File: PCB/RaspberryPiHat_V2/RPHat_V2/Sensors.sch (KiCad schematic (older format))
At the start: 19 parts, among them IC1 TXB0108YZPR2, J2 Hall effect connector Right, J3 Halleffect Connector Left, U1 BME680, U2 INA219AxD, U3 ICM-20948, U4 GY-NEO6MV2

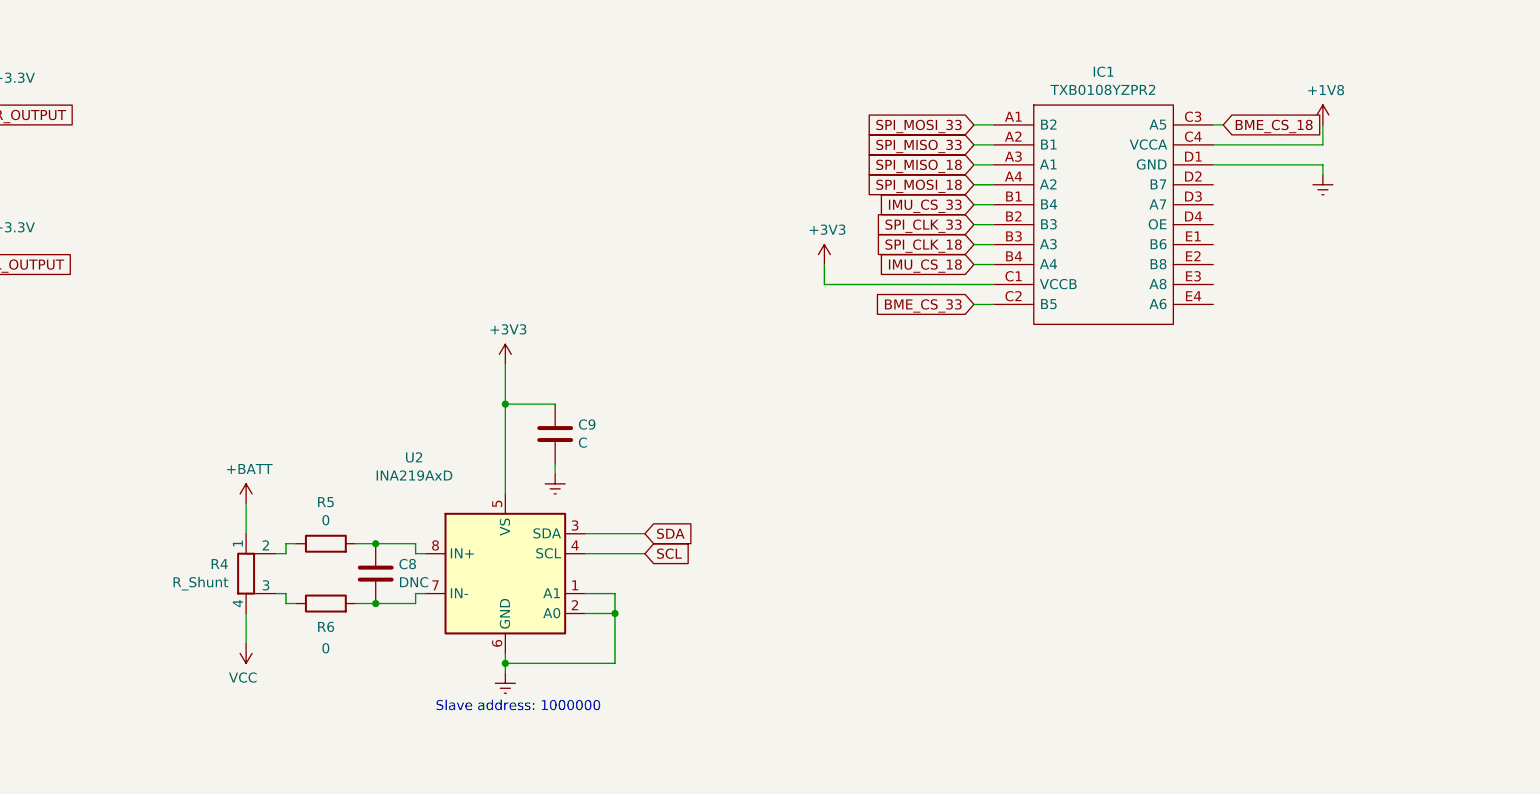
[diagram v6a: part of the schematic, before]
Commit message: Added footprints to all componetns
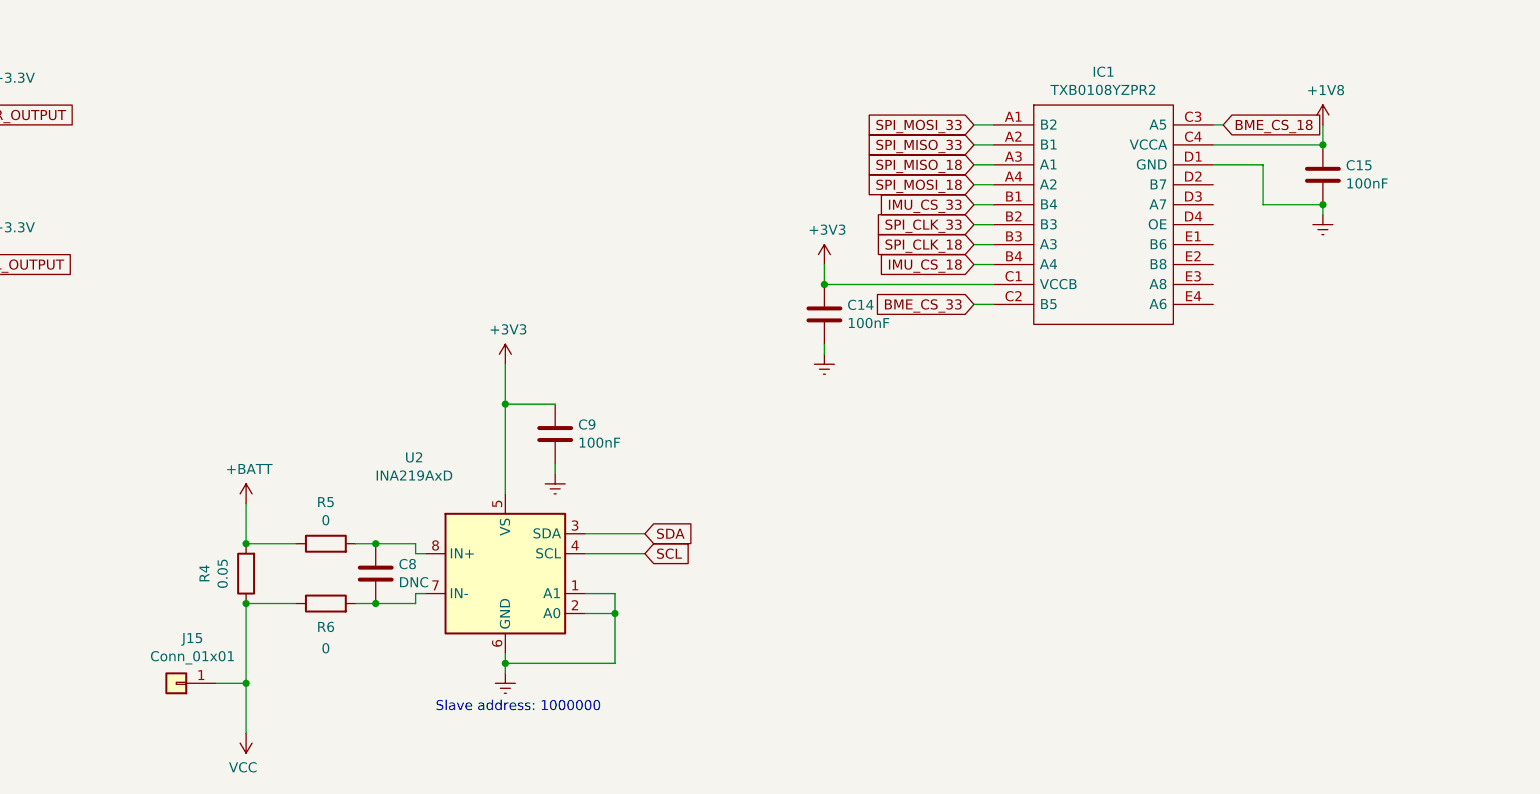
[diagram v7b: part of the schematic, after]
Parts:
- removed R4: R_Shunt, symbol Device:R_Shunt
- added C14, C15: 100nF, Capacitor_SMD:C_0603_1608Metric_Pad1.08x0.95mm_HandSolder, symbol Device:C
- added J15: Conn_01x01, Connector_Pin:Pin_D1.3mm_L11.0mm, symbol Connector_Generic:Conn_01x01
- added R4: 0.05, User:CSS2H-3920, symbol Device:R
- C10, C11, C12, C6, C7: footprint Capacitor_SMD:C_0805_2012Metric_Pad1.18x1.45mm_HandSolder -> Capacitor_SMD:C_0603_1608Metric_Pad1.08x0.95mm_HandSolder
- C8: footprint (none) -> Capacitor_SMD:C_0603_1608Metric_Pad1.08x0.95mm_HandSolder
- C9: value C -> 100nF; footprint (none) -> Capacitor_SMD:C_0603_1608Metric_Pad1.08x0.95mm_HandSolder
- IC1: footprint BGA20C50P4X5_189X239X50 -> TXB0108YZPR2:BGA20C50P4X5_189X239X50
- R5, R6: footprint (none) -> Resistor_SMD:R_0603_1608Metric_Pad0.98x0.95mm_HandSolder
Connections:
- net +1V8: now also C15.1
- net +3V3: now also C14.1
- net +BATT: now also R5.1, R4.2
- net GNDREF: now also C14.2, C15.2
- net VCC: now also R6.1, J15.1 (Pin_1), R4.1
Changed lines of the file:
@@
 F 0 "C7" H 1615 1496 50  0000 L CNN
 F 1 "100nF" H 1615 1405 50  0000 L CNN
-F 2 "Capacitor_SMD:C_0805_2012Metric_Pad1.18x1.45mm_HandSolder" H 1538 1300 50  0001 C CNN
+F 2 "Capacitor_SMD:C_0603_1608Metric_Pad1.08x0.95mm_HandSolder" H 1538 1300 50  0001 C CNN
 F 3 "~" H 1500 1450 50  0001 C CNN
 	1    1500 1450
@@
 F 0 "C6" H 1165 1496 50  0000 L CNN
 F 1 "100nF" H 1165 1405 50  0000 L CNN
-F 2 "Capacitor_SMD:C_0805_2012Metric_Pad1.18x1.45mm_HandSolder" H 1088 1300 50  0001 C CNN
+F 2 "Capacitor_SMD:C_0603_1608Metric_Pad1.08x0.95mm_HandSolder" H 1088 1300 50  0001 C CNN
 F 3 "~" H 1050 1450 50  0001 C CNN
 	1    1050 1450
@@
 F 0 "C11" H 7815 2246 50  0000 L CNN
 F 1 "100nF" H 7815 2155 50  0000 L CNN
-F 2 "Capacitor_SMD:C_0805_2012Metric_Pad1.18x1.45mm_HandSolder" H 7738 2050 50  0001 C CNN
+F 2 "Capacitor_SMD:C_0603_1608Metric_Pad1.08x0.95mm_HandSolder" H 7738 2050 50  0001 C CNN
 F 3 "~" H 7700 2200 50  0001 C CNN
 	1    7700 2200
@@
 F 0 "C10" H 7765 1446 50  0000 L CNN
 F 1 "100nF" H 7765 1355 50  0000 L CNN
-F 2 "Capacitor_SMD:C_0805_2012Metric_Pad1.18x1.45mm_HandSolder" H 7688 1250 50  0001 C CNN
+F 2 "Capacitor_SMD:C_0603_1608Metric_Pad1.08x0.95mm_HandSolder" H 7688 1250 50  0001 C CNN
 F 3 "~" H 7650 1400 50  0001 C CNN
 	1    7650 1400
@@
 F 0 "C12" H 8215 1446 50  0000 L CNN
 F 1 "100nF" H 8215 1355 50  0000 L CNN
-F 2 "Capacitor_SMD:C_0805_2012Metric_Pad1.18x1.45mm_HandSolder" H 8138 1250 50  0001 C CNN
+F 2 "Capacitor_SMD:C_0603_1608Metric_Pad1.08x0.95mm_HandSolder" H 8138 1250 50  0001 C CNN
 F 3 "~" H 8100 1400 50  0001 C CNN
 	1    8100 1400
@@
 F 0 "IC1" H 7000 4065 50  0000 C CNN
 F 1 "TXB0108YZPR2" H 7000 3974 50  0000 C CNN
-F 2 "BGA20C50P4X5_189X239X50" H 7400 3900 50  0001 L CNN
+F 2 "TXB0108YZPR2:BGA20C50P4X5_189X239X50" H 7400 3900 50  0001 L CNN
 F 3 "http://www.ti.com/lit/gpn/TXB0108" H 7400 3800 50  0001 L CNN
 F 4 "8-Bit Bidirectional Voltage-Level Shifter with Auto Direction Sensing and +/-15-kV ESD Protect" H 7400 3700 50  0001 L CNN "Description"
@@
 Wire Wire Line
 	8100 3900 8100 3800
-$Comp
-L power:GNDREF #PWR0132
-U 1 1 609C7438
-P 8100 4050
-F 0 "#PWR0132" H 8100 3800 50  0001 C CNN
-F 1 "GNDREF" H 8105 3877 50  0001 C CNN
-F 2 "" H 8100 4050 50  0001 C CNN
-F 3 "" H 8100 4050 50  0001 C CNN
-	1    8100 4050
-	1    0    0    -1
-$EndComp
-Wire Wire Line
-	8100 4000 8100 4050
 Wire Wire Line
 	7550 3900 8100 3900
-Wire Wire Line
-	7550 4000 8100 4000
 Text GLabel 6350 4000 0    50   Input ~ 0
 SPI_MISO_18
@@
 P 4250 5350
 F 0 "C9" H 4365 5396 50  0000 L CNN
-F 1 "C" H 4365 5305 50  0000 L CNN
-F 2 "" H 4288 5200 50  0001 C CNN
+F 1 "100nF" H 4365 5305 50  0000 L CNN
+F 2 "Capacitor_SMD:C_0603_1608Metric_Pad1.08x0.95mm_HandSolder" H 4288 5200 50  0001 C CNN
 F 3 "~" H 4250 5350 50  0001 C CNN
 	1    4250 5350
@@
 	4250 5500 4250 5550
 $Comp
-L Device:R_Shunt R4
-U 1 1 60A2AE3C
-P 2700 6050
-F 0 "R4" H 2612 6096 50  0000 R CNN
-F 1 "R_Shunt" H 2612 6005 50  0000 R CNN
-F 2 "" V 2630 6050 50  0001 C CNN
-F 3 "~" H 2700 6050 50  0001 C CNN
-	1    2700 6050
-	1    0    0    -1
-$EndComp
-$Comp
 L Device:R R5
 U 1 1 60A32138
@@
 F 0 "R5" V 3307 5900 50  0000 C CNN
 F 1 "0" V 3216 5900 50  0000 C CNN
-F 2 "" V 3030 5900 50  0001 C CNN
+F 2 "Resistor_SMD:R_0603_1608Metric_Pad0.98x0.95mm_HandSolder" V 3030 5900 50  0001 C CNN
 F 3 "~" H 3100 5900 50  0001 C CNN
 	1    3100 5900
@@
 F 0 "R6" V 2981 6200 50  0000 C CNN
 F 1 "0" V 2903 6200 50  0000 C BNN
-F 2 "" V 3030 6200 50  0001 C CNN
+F 2 "Resistor_SMD:R_0603_1608Metric_Pad0.98x0.95mm_HandSolder" V 3030 6200 50  0001 C CNN
 F 3 "~" H 3100 6200 50  0001 C CNN
 	1    3100 6200
@@
 F 0 "C8" H 3465 6096 50  0000 L CNN
 F 1 "DNC" H 3465 6005 50  0000 L CNN
-F 2 "" H 3388 5900 50  0001 C CNN
+F 2 "Capacitor_SMD:C_0603_1608Metric_Pad1.08x0.95mm_HandSolder" H 3388 5900 50  0001 C CNN
 F 3 "~" H 3350 6050 50  0001 C CNN
 	1    3350 6050
 	1    0    0    -1
 $EndComp
-Wire Wire Line
-	2850 6150 2900 6150
-Wire Wire Line
-	2900 6150 2900 6200
-Wire Wire Line
-	2900 6200 2950 6200
-Wire Wire Line
-	2850 5950 2900 5950
-Wire Wire Line
-	2900 5950 2900 5900
-Wire Wire Line
-	2900 5900 2950 5900
 Wire Wire Line
 	3250 5900 3350 5900
@@
 	1    0    0    -1
 $EndComp
-Wire Wire Line
-	2700 5700 2700 5850
 $Comp
 L power:VCC #PWR0137
 U 1 1 60A5EBF9
-P 2700 6400
-F 0 "#PWR0137" H 2700 6250 50  0001 C CNN
-F 1 "VCC" H 2715 6573 50  0000 C CNN
-F 2 "" H 2700 6400 50  0001 C CNN
-F 3 "" H 2700 6400 50  0001 C CNN
-	1    2700 6400
+P 2700 6850
+F 0 "#PWR0137" H 2700 6700 50  0001 C CNN
+F 1 "VCC" H 2715 7023 50  0000 C CNN
+F 2 "" H 2700 6850 50  0001 C CNN
+F 3 "" H 2700 6850 50  0001 C CNN
+	1    2700 6850
 	-1   0    0    1
 $EndComp
-Wire Wire Line
-	2700 6250 2700 6400
 Wire Wire Line
 	4400 6150 4550 6150
@@
 	1050 1650 1300 1650
 Connection ~ 1300 1650
+$Comp
+L Device:C C14
+U 1 1 60AB39EC
+P 5600 4750
+F 0 "C14" H 5715 4796 50  0000 L CNN
+F 1 "100nF" H 5715 4705 50  0000 L CNN
+F 2 "Capacitor_SMD:C_0603_1608Metric_Pad1.08x0.95mm_HandSolder" H 5638 4600 50  0001 C CNN
+F 3 "~" H 5600 4750 50  0001 C CNN
+	1    5600 4750
+	1    0    0    -1
+$EndComp
+$Comp
+L Device:C C15
+U 1 1 60AB76A4
+P 8100 4050
+F 0 "C15" H 8215 4096 50  0000 L CNN
+F 1 "100nF" H 8215 4005 50  0000 L CNN
+F 2 "Capacitor_SMD:C_0603_1608Metric_Pad1.08x0.95mm_HandSolder" H 8138 3900 50  0001 C CNN
+F 3 "~" H 8100 4050 50  0001 C CNN
+	1    8100 4050
+	1    0    0    -1
+$EndComp
+$Comp
+L power:GNDREF #PWR01
+U 1 1 60ABB27E
+P 5600 4950
+F 0 "#PWR01" H 5600 4700 50  0001 C CNN
+F 1 "GNDREF" H 5605 4777 50  0001 C CNN
+F 2 "" H 5600 4950 50  0001 C CNN
+F 3 "" H 5600 4950 50  0001 C CNN
+	1    5600 4950
+	1    0    0    -1
+$EndComp
+Wire Wire Line
+	5600 4900 5600 4950
+Connection ~ 8100 3900
+$Comp
+L power:GNDREF #PWR02
+U 1 1 60ACAE6A
+P 8100 4250
+F 0 "#PWR02" H 8100 4000 50  0001 C CNN
+F 1 "GNDREF" H 8105 4077 50  0001 C CNN
+F 2 "" H 8100 4250 50  0001 C CNN
+F 3 "" H 8100 4250 50  0001 C CNN
+	1    8100 4250
+	1    0    0    -1
+$EndComp
+Wire Wire Line
+	8100 4200 8100 4250
+Wire Wire Line
+	7550 4000 7800 4000
+Wire Wire Line
+	7800 4000 7800 4200
+Wire Wire Line
+	7800 4200 8100 4200
+Connection ~ 8100 4200
+Connection ~ 5600 4600
+$Comp
+L Device:R R4
+U 1 1 60AE3FA9
+P 2700 6050
+F 0 "R4" V 2907 6050 50  0000 C CNN
+F 1 "0.05" V 2816 6050 50  0000 C CNN
+F 2 "User:CSS2H-3920" V 2630 6050 50  0001 C CNN
+F 3 "~" H 2700 6050 50  0001 C CNN
+	1    2700 6050
+	-1   0    0    1
+$EndComp
+Wire Wire Line
+	2700 5700 2700 5900
+Wire Wire Line
+	2950 5900 2700 5900
+Connection ~ 2700 5900
+Wire Wire Line
+	2950 6200 2700 6200
+Connection ~ 2700 6200
+Wire Wire Line
+	2700 6200 2700 6600
+$Comp
+L Connector_Generic:Conn_01x01 J15
+U 1 1 60B5A1C5
+P 2350 6600
+F 0 "J15" H 2268 6375 50  0000 C CNN
+F 1 "Conn_01x01" H 2268 6466 50  0000 C CNN
+F 2 "Connector_Pin:Pin_D1.3mm_L11.0mm" H 2350 6600 50  0001 C CNN
+F 3 "~" H 2350 6600 50  0001 C CNN
+	1    2350 6600
+	-1   0    0    1
+$EndComp
+Wire Wire Line
+	2550 6600 2700 6600
+Connection ~ 2700 6600
+Wire Wire Line
+	2700 6600 2700 6850
 $EndSCHEMATC

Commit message: started pcb routing
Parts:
- removed IC1: TXB0108YZPR2, TXB0108YZPR2:BGA20C50P4X5_189X239X50, symbol RPHat_V2-rescue:TXB0108YZPR2-TXB0108YZPR2
- added IC1: TXB0108DQSR, User:TXB0108DQSR, symbol User:TXB0108DQSR
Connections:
- net +1V8: now also IC1.5 (VCCA), IC1.6 (OE)
- net +3V3: now also IC1.16 (VCCB)
- net BME_CS_18: now also IC1.14 (B5)
- net BME_CS_33: now also IC1.7 (A5)
- net IMU_CS_18: now also IC1.17 (B4)
- net IMU_CS_33: now also IC1.4 (A4)
- net SPI_CLK_18: now also IC1.18 (B3)
- net SPI_CLK_33: now also IC1.3 (A3)
- net SPI_MISO_18: now also IC1.19 (B2)
- net SPI_MISO_33: now also IC1.2 (A2)
- net SPI_MOSI_18: now also IC1.20 (B1)
- net SPI_MOSI_33: now also IC1.1 (A1)
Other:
- moved on the sheet: C14, C15
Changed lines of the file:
@@
 HE_R_OUTPUT
-$Comp
-L RPHat_V2-rescue:TXB0108YZPR2-TXB0108YZPR2 IC1
-U 1 1 60A9D2C1
-P 6450 3800
-F 0 "IC1" H 7000 4065 50  0000 C CNN
-F 1 "TXB0108YZPR2" H 7000 3974 50  0000 C CNN
-F 2 "TXB0108YZPR2:BGA20C50P4X5_189X239X50" H 7400 3900 50  0001 L CNN
-F 3 "http://www.ti.com/lit/gpn/TXB0108" H 7400 3800 50  0001 L CNN
-F 4 "8-Bit Bidirectional Voltage-Level Shifter with Auto Direction Sensing and +/-15-kV ESD Protect" H 7400 3700 50  0001 L CNN "Description"
-F 5 "0.5" H 7400 3600 50  0001 L CNN "Height"
-F 6 "Texas Instruments" H 7400 3500 50  0001 L CNN "Manufacturer_Name"
-F 7 "TXB0108YZPR2" H 7400 3400 50  0001 L CNN "Manufacturer_Part_Number"
-F 8 "595-TXB0108YZPR2" H 7400 3300 50  0001 L CNN "Mouser Part Number"
-F 9 "https://www.mouser.co.uk/ProductDetail/Texas-Instruments/TXB0108YZPR2?qs=PqoDHHvF64977Sea9xf4wg%3D%3D" H 7400 3200 50  0001 L CNN "Mouser Price/Stock"
-F 10 "TXB0108YZPR2" H 7400 3100 50  0001 L CNN "Arrow Part Number"
-F 11 "https://www.arrow.com/en/products/txb0108yzpr2/texas-instruments" H 7400 3000 50  0001 L CNN "Arrow Price/Stock"
-	1    6450 3800
-	1    0    0    -1
-$EndComp
 $Comp
 L power:+1V8 #PWR0130
 U 1 1 609C23EB
-P 8100 3800
-F 0 "#PWR0130" H 8100 3650 50  0001 C CNN
-F 1 "+1V8" H 8115 3973 50  0000 C CNN
-F 2 "" H 8100 3800 50  0001 C CNN
-F 3 "" H 8100 3800 50  0001 C CNN
-	1    8100 3800
+P 5650 5300
+F 0 "#PWR0130" H 5650 5150 50  0001 C CNN
+F 1 "+1V8" H 5665 5473 50  0000 C CNN
+F 2 "" H 5650 5300 50  0001 C CNN
+F 3 "" H 5650 5300 50  0001 C CNN
+	1    5650 5300
 	1    0    0    -1
 $EndComp
@@
 L power:+3V3 #PWR0131
 U 1 1 609C3DE0
-P 5600 4500
-F 0 "#PWR0131" H 5600 4350 50  0001 C CNN
-F 1 "+3V3" H 5615 4673 50  0000 C CNN
-F 2 "" H 5600 4500 50  0001 C CNN
-F 3 "" H 5600 4500 50  0001 C CNN
-	1    5600 4500
-	1    0    0    -1
-$EndComp
-Wire Wire Line
-	5600 4600 5600 4500
-Wire Wire Line
-	8100 3900 8100 3800
-Wire Wire Line
-	7550 3900 8100 3900
-Text GLabel 6350 4000 0    50   Input ~ 0
-SPI_MISO_18
-Text GLabel 6350 4100 0    50   Input ~ 0
-SPI_MOSI_18
-Text GLabel 6350 4400 0    50   Input ~ 0
+P 8550 5400
+F 0 "#PWR0131" H 8550 5250 50  0001 C CNN
+F 1 "+3V3" H 8565 5573 50  0000 C CNN
+F 2 "" H 8550 5400 50  0001 C CNN
+F 3 "" H 8550 5400 50  0001 C CNN
+	1    8550 5400
+	1    0    0    -1
+$EndComp
+Wire Wire Line
+	5650 5400 5650 5300
+Text GLabel 7800 5700 2    50   Input ~ 0
 SPI_CLK_18
-Text GLabel 6350 4500 0    50   Input ~ 0
+Text GLabel 7800 5600 2    50   Input ~ 0
 IMU_CS_18
-Text GLabel 7600 3800 2    50   Input ~ 0
+Text GLabel 7750 5300 2    50   Input ~ 0
 BME_CS_18
-Text GLabel 6350 3900 0    50   Input ~ 0
+Text GLabel 6500 5100 0    50   Input ~ 0
 SPI_MISO_33
-Text GLabel 6350 3800 0    50   Input ~ 0
+Text GLabel 6500 5000 0    50   Input ~ 0
 SPI_MOSI_33
-Text GLabel 6350 4300 0    50   Input ~ 0
+Text GLabel 6500 5200 0    50   Input ~ 0
 SPI_CLK_33
-Text GLabel 6350 4200 0    50   Input ~ 0
+Text GLabel 6500 5300 0    50   Input ~ 0
 IMU_CS_33
-Text GLabel 6350 4700 0    50   Input ~ 0
+Text GLabel 6500 5600 0    50   Input ~ 0
 BME_CS_33
 Wire Wire Line
-	5600 4600 6450 4600
-Wire Wire Line
-	7600 3800 7550 3800
-Wire Wire Line
-	6350 4000 6450 4000
-Wire Wire Line
-	6350 4100 6450 4100
-Wire Wire Line
-	6350 4400 6450 4400
-Wire Wire Line
-	6350 4500 6450 4500
-Wire Wire Line
-	6350 3800 6450 3800
-Wire Wire Line
-	6350 3900 6450 3900
-Wire Wire Line
-	6350 4200 6450 4200
-Wire Wire Line
-	6350 4300 6450 4300
-Wire Wire Line
-	6350 4700 6450 4700
+	7750 5300 7700 5300
+Wire Wire Line
+	7800 5800 7700 5800
+Wire Wire Line
+	7800 5900 7700 5900
+Wire Wire Line
+	7800 5700 7700 5700
+Wire Wire Line
+	7800 5600 7700 5600
+Wire Wire Line
+	6500 5000 6600 5000
+Wire Wire Line
+	6500 5100 6600 5100
+Wire Wire Line
+	6500 5300 6600 5300
+Wire Wire Line
+	6500 5200 6600 5200
+Wire Wire Line
+	6500 5600 6600 5600
 Text GLabel 4700 5850 2    50   Input ~ 0
 SDA
@@
 L Device:C C14
 U 1 1 60AB39EC
-P 5600 4750
-F 0 "C14" H 5715 4796 50  0000 L CNN
-F 1 "100nF" H 5715 4705 50  0000 L CNN
-F 2 "Capacitor_SMD:C_0603_1608Metric_Pad1.08x0.95mm_HandSolder" H 5638 4600 50  0001 C CNN
-F 3 "~" H 5600 4750 50  0001 C CNN
-	1    5600 4750
+P 8550 5650
+F 0 "C14" H 8665 5696 50  0000 L CNN
+F 1 "100nF" H 8665 5605 50  0000 L CNN
+F 2 "Capacitor_SMD:C_0603_1608Metric_Pad1.08x0.95mm_HandSolder" H 8588 5500 50  0001 C CNN
+F 3 "~" H 8550 5650 50  0001 C CNN
+	1    8550 5650
 	1    0    0    -1
 $EndComp
@@
 L Device:C C15
 U 1 1 60AB76A4
-P 8100 4050
-F 0 "C15" H 8215 4096 50  0000 L CNN
-F 1 "100nF" H 8215 4005 50  0000 L CNN
-F 2 "Capacitor_SMD:C_0603_1608Metric_Pad1.08x0.95mm_HandSolder" H 8138 3900 50  0001 C CNN
-F 3 "~" H 8100 4050 50  0001 C CNN
-	1    8100 4050
+P 5650 5550
+F 0 "C15" H 5765 5596 50  0000 L CNN
+F 1 "100nF" H 5765 5505 50  0000 L CNN
+F 2 "Capacitor_SMD:C_0603_1608Metric_Pad1.08x0.95mm_HandSolder" H 5688 5400 50  0001 C CNN
+F 3 "~" H 5650 5550 50  0001 C CNN
+	1    5650 5550
 	1    0    0    -1
 $EndComp
@@
 L power:GNDREF #PWR01
 U 1 1 60ABB27E
-P 5600 4950
-F 0 "#PWR01" H 5600 4700 50  0001 C CNN
-F 1 "GNDREF" H 5605 4777 50  0001 C CNN
-F 2 "" H 5600 4950 50  0001 C CNN
-F 3 "" H 5600 4950 50  0001 C CNN
-	1    5600 4950
-	1    0    0    -1
-$EndComp
-Wire Wire Line
-	5600 4900 5600 4950
-Connection ~ 8100 3900
+P 8550 5850
+F 0 "#PWR01" H 8550 5600 50  0001 C CNN
+F 1 "GNDREF" H 8555 5677 50  0001 C CNN
+F 2 "" H 8550 5850 50  0001 C CNN
+F 3 "" H 8550 5850 50  0001 C CNN
+	1    8550 5850
+	1    0    0    -1
+$EndComp
+Wire Wire Line
+	8550 5800 8550 5850
 $Comp
 L power:GNDREF #PWR02
 U 1 1 60ACAE6A
-P 8100 4250
-F 0 "#PWR02" H 8100 4000 50  0001 C CNN
-F 1 "GNDREF" H 8105 4077 50  0001 C CNN
-F 2 "" H 8100 4250 50  0001 C CNN
-F 3 "" H 8100 4250 50  0001 C CNN
-	1    8100 4250
-	1    0    0    -1
-$EndComp
-Wire Wire Line
-	8100 4200 8100 4250
-Wire Wire Line
-	7550 4000 7800 4000
-Wire Wire Line
-	7800 4000 7800 4200
-Wire Wire Line
-	7800 4200 8100 4200
-Connection ~ 8100 4200
-Connection ~ 5600 4600
+P 5650 5750
+F 0 "#PWR02" H 5650 5500 50  0001 C CNN
+F 1 "GNDREF" H 5655 5577 50  0001 C CNN
+F 2 "" H 5650 5750 50  0001 C CNN
+F 3 "" H 5650 5750 50  0001 C CNN
+	1    5650 5750
+	1    0    0    -1
+$EndComp
+Wire Wire Line
+	5650 5700 5650 5750
 $Comp
 L Device:R R4
@@
 Wire Wire Line
 	2700 6600 2700 6850
+$Comp
+L User:TXB0108DQSR IC1
+U 1 1 60AA4FBA
+P 6600 5000
+F 0 "IC1" H 7150 5265 50  0000 C CNN
+F 1 "TXB0108DQSR" H 7150 5174 50  0000 C CNN
+F 2 "User:TXB0108DQSR" H 7550 5100 50  0001 L CNN
+F 3 "http://www.ti.com/lit/gpn/txb0108" H 7550 5000 50  0001 L CNN
+F 4 "8-Bit Bidirectional Voltage-Level Shifter with Auto Direction Sensing and +/-15-kV ESD Protect" H 7550 4900 50  0001 L CNN "Description"
+F 5 "0" H 7550 4800 50  0001 L CNN "Height"
+F 6 "Texas Instruments" H 7550 4700 50  0001 L CNN "Manufacturer_Name"
+F 7 "TXB0108DQSR" H 7550 4600 50  0001 L CNN "Manufacturer_Part_Number"
+F 8 "595-TXB0108DQSR" H 7550 4500 50  0001 L CNN "Mouser Part Number"
+F 9 "https://www.mouser.co.uk/ProductDetail/Texas-Instruments/TXB0108DQSR?qs=EuM%2FBx4ov4SMZCOlCh%2FWxA%3D%3D" H 7550 4400 50  0001 L CNN "Mouser Price/Stock"
+F 10 "TXB0108DQSR" H 7550 4300 50  0001 L CNN "Arrow Part Number"
+F 11 "https://www.arrow.com/en/products/txb0108dqsr/texas-instruments" H 7550 4200 50  0001 L CNN "Arrow Price/Stock"
+	1    6600 5000
+	1    0    0    -1
+$EndComp
+Wire Wire Line
+	8550 5500 8550 5400
+Connection ~ 8550 5500
+Text GLabel 7800 5900 2    50   Input ~ 0
+SPI_MOSI_18
+Text GLabel 7800 5800 2    50   Input ~ 0
+SPI_MISO_18
+Wire Wire Line
+	7700 5500 8550 5500
+Wire Wire Line
+	6600 5500 6500 5500
+Wire Wire Line
+	6500 5500 6500 5400
+Wire Wire Line
+	6500 5400 6600 5400
+Wire Wire Line
+	6500 5400 5650 5400
+Connection ~ 6500 5400
+Connection ~ 5650 5400
 $EndSCHEMATC
